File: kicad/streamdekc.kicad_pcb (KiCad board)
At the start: 2 copper layers, 26 parts, among them IC1 74HC4051P, IC2 74HC4051P, SW1 SW_DIP_x01, SW2 SW_DIP_x01, SW3 SW_DIP_x01, SW4 SW_DIP_x01, SW5 SW_DIP_x01, SW6 SW_DIP_x01, SW7 SW_DIP_x01, SW8 SW_DIP_x01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

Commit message: whee
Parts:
- IC1, IC2, U1_1, U1_2, U2_1, U2_2: moved to B.Cu
- moved U1_2 124.5 mm to (82.3, 131.2), turned to -90 degrees
- moved U1_1 116.6 mm to (82.3, 116.0), turned to -90 degrees
- moved U2_2 88.2 mm to (85.0, 106.5), turned to -90 degrees
- moved IC2 87.3 mm to (151.6, 92.7), turned to -90 degrees
- moved IC1 86.3 mm to (116.5, 92.5), turned to -90 degrees
- moved U2_1 72.1 mm to (85.0, 96.2), turned to -90 degrees
- moved SW8 9.50 mm to (207.5, 138.0)

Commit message: Initial pcb design
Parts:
- added REF**: MountingHole_4.3mm_M4_DIN965_Pad, MountingHole:MountingHole_4.3mm_M4_DIN965_Pad, F.Cu at (67.0, 123.5)
- added REF**: MountingHole_4.3mm_M4_DIN965_Pad, MountingHole:MountingHole_4.3mm_M4_DIN965_Pad, F.Cu at (239.0, 68.0)
- added REF**: MountingHole_4.3mm_M4_DIN965_Pad, MountingHole:MountingHole_4.3mm_M4_DIN965_Pad, F.Cu at (67.0, 68.0)
- added REF**: MountingHole_4.3mm_M4_DIN965_Pad, MountingHole:MountingHole_4.3mm_M4_DIN965_Pad, F.Cu at (239.0, 123.5)
- moved IC2 61.7 mm to (91.6, 106.9)
- moved DISP7 33.0 mm to (144.4, 99.7)
- moved U2_2 32.5 mm to (79.5, 74.5), turned to 90 degrees
- moved DISP6 32.1 mm to (112.4, 99.7)
- moved SW3 31.9 mm to (148.2, 92.2)
- moved SW8 31.5 mm to (180.2, 122.2)
- moved DISP5 30.9 mm to (80.4, 99.7)
- moved DISP8 30.8 mm to (176.4, 99.7)
- moved DISP3 30.8 mm to (144.4, 69.7)
- moved SW2 29.9 mm to (116.2, 92.2)
- moved SW4 29.7 mm to (180.2, 92.2)
- moved DISP2 29.5 mm to (112.4, 69.7)
- moved IC1 29.4 mm to (91.1, 77.7)
- moved SW7 29.2 mm to (148.2, 122.2)
- moved DISP4 29.1 mm to (176.4, 69.7)
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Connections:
- SW1 pad 1: unconnected-(SW1-Pad1) -> /SW1
- SW2 pad 1: unconnected-(SW2-Pad1) -> /SW2
- SW3 pad 1: unconnected-(SW3-Pad1) -> /SW3
- SW4 pad 1: unconnected-(SW4-Pad1) -> /SW4
- SW5 pad 1: unconnected-(SW5-Pad1) -> /SW5
- SW6 pad 1: unconnected-(SW6-Pad1) -> /SW6
- SW7 pad 1: unconnected-(SW7-Pad1) -> /SW7
- SW8 pad 1: unconnected-(SW8-Pad1) -> /SW8
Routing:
- net /3V3: track 0.00 -> 292.3 mm, vias 0 -> 1
- net /SCL_5V: track 0.00 -> 257.9 mm, vias 0 -> 1
- net /A3: track 0.00 -> 227.1 mm, vias 0 -> 1
- net /A2: track 0.00 -> 221.4 mm, vias 0 -> 3
- net /A1: track 0.00 -> 212.3 mm, vias 0 -> 3
- net /A0: track 0.00 -> 203.2 mm, vias 0 -> 3
- net /DISP_8_SDA: track 0.00 -> 109.4 mm, vias 0 -> 1
- net /DISP_4_SDA: track 0.00 -> 103.6 mm, vias 0 -> 1
- net /SW4: track 0.00 -> 91.1 mm, vias 0 -> 2
- net /D10: track 0.00 -> 90.8 mm, vias 0 -> 2
- net /D8: track 0.00 -> 90.7 mm, vias 0 -> 2
- net /D9: track 0.00 -> 90.6 mm, vias 0 -> 2
- net /SW3: track 0.00 -> 88.6 mm, vias 0 -> 1
- net /SW8: track 0.00 -> 84.2 mm
- net /DISP_7_SDA: track 0.00 -> 79.5 mm, vias 0 -> 2
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- added copper zone on F.Cu, net /5V
- added copper zone on B.Cu, net /GND
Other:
- board outline added: 184 x 67.5 mm
- board text added: "Order of Assembly: 1. Switches 2. ICs 3. Power Converter 4. Slide Potentiometers 5. Qt Py 6. Displays (Good luck)"
- board text added: "Streamdekc Designed by Mark Hutcheson April 2022"

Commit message: Move QtPy for easier (aka physically possible) assembly
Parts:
- moved U1_1 5.27 mm to (64.5, 102.2)
- moved U1_2 5.27 mm to (64.5, 117.5)
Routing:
- net /D6: track 28.2 -> 35.3 mm, vias 2 -> 3
- net /A3: track 227.1 -> 221.8 mm, vias 1 -> 3
- net /SDA: track 13.2 -> 18.5 mm, vias 0 -> 1
- net /SCL: track 13.4 -> 18.7 mm, vias 0 -> 1
- net /A2: track 221.4 -> 216.1 mm
- net /A1: track 212.3 -> 207.0 mm
- net /A0: track 203.2 -> 198.0 mm
- net /D10: track 90.8 -> 94.7 mm
- net /3V3: track 292.3 -> 295.9 mm, vias 1 -> 2
- net /SCL_5V: track 257.9 -> 261.4 mm
- net /D9: track 90.6 -> 93.2 mm
- net /SW1: track 44.4 -> 46.5 mm
- net /D8: track 90.7 -> 92.3 mm
- net /DISP_5_SDA: track 23.3 -> 24.5 mm
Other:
- board text added: "Order of Assembly: 1. Switches 2. ICs 3. Power Converter 4. Slide Potentiometers 5. Qt Py 6. Displays"
- board text removed: "Order of Assembly: 1. Switches 2. ICs 3. Power Converter 4. Slide Potentiometers 5. Qt Py 6. Displays (Good luck)"

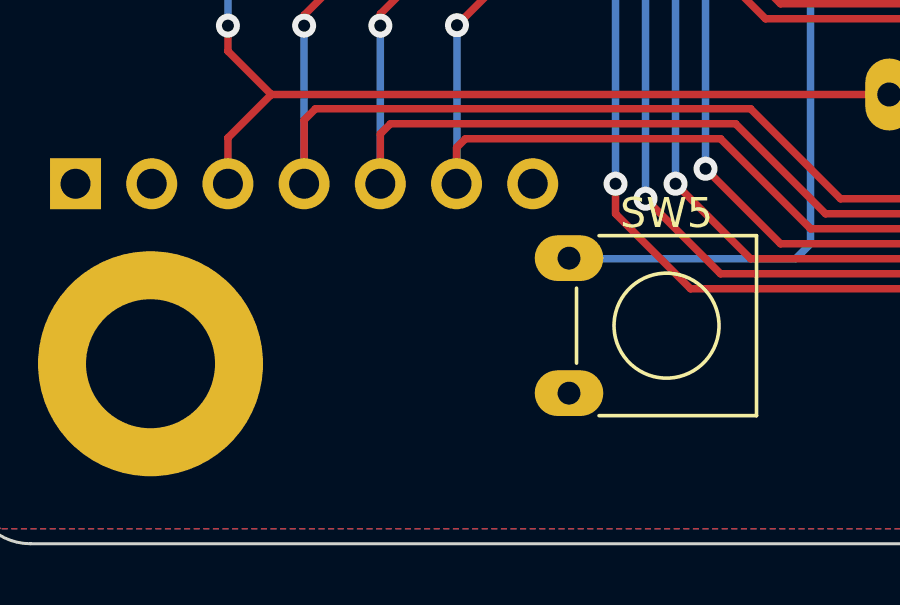
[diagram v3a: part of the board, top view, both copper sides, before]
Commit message: Update assembly instructions on B.Silkscreen
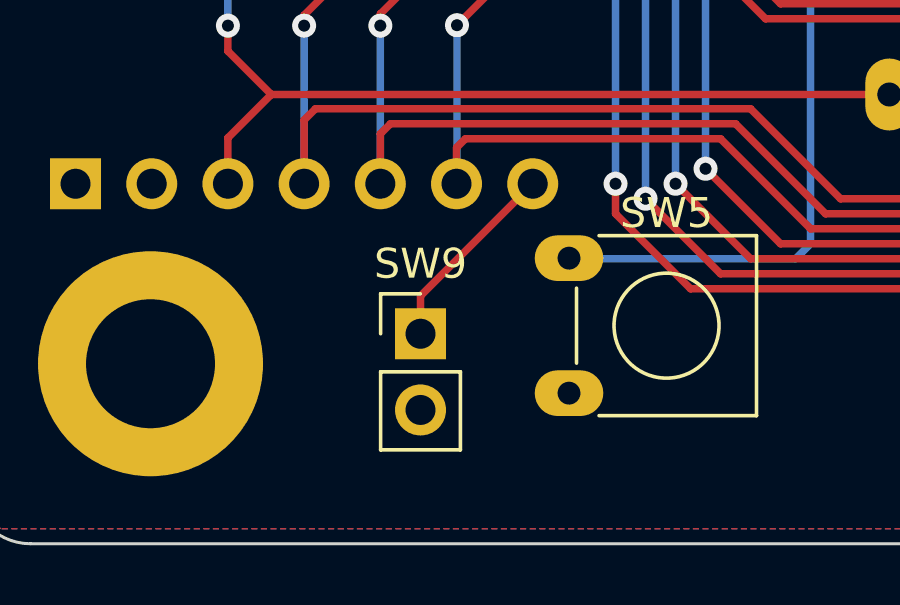
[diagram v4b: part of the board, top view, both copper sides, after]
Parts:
- added SW9: SW_DIP_x01, Connector_PinHeader_2.54mm:PinHeader_1x02_P2.54mm_Vertical, F.Cu at (76.0, 122.5)
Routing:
- net /D7: track 0.00 -> 6.55 mm
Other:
- board text added: "Order of Assembly: 1. Switches 2. ICs 3. Power Converter 4. Slide Potentiometers 5. Qt Py 6. Extra Pin Header 7. Displays"
- board text removed: "Order of Assembly: 1. Switches 2. ICs 3. Power Converter 4. Slide Potentiometers 5. Qt Py 6. Displays"
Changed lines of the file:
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@@
   (net 39 "unconnected-(U2_2-Pad4)")
   (net 40 "unconnected-(U2_2-Pad5)")
+  (footprint "Connector_PinHeader_2.54mm:PinHeader_1x02_P2.54mm_Vertical" (layer "F.Cu")
+    (at 76 122.5)
+    (descr "Through hole straight pin header, 1x02, 2.54mm pitch, single row")
+    (tags "Through hole pin header THT 1x02 2.54mm single row")
+    (property "Sheetfile" "streamdekc.kicad_sch")
+    (property "Sheetname" "")
+    (attr through_hole)
+    (fp_text reference "SW9" (at 0 -2.33) (layer "F.SilkS")
+      (effects (font (size 1 1) (thickness 0.15)))
+    )
+    (fp_text value "SW_DIP_x01" (at 0 4.87) (layer "F.Fab")
+      (effects (font (size 1 1) (thickness 0.15)))
+    )
+    (fp_text user "${REFERENCE}" (at 0 1.27 90) (layer "F.Fab")
+      (effects (font (size 1 1) (thickness 0.15)))
+    )
+    (fp_line (start -1.33 1.27) (end 1.33 1.27) (layer "F.SilkS") (width 0.12))
+    (fp_line (start -1.33 1.27) (end -1.33 3.87) (layer "F.SilkS") (width 0.12))
+    (fp_line (start -1.33 -1.33) (end 0 -1.33) (layer "F.SilkS") (width 0.12))
+    (fp_line (start 1.33 1.27) (end 1.33 3.87) (layer "F.SilkS") (width 0.12))
+    (fp_line (start -1.33 3.87) (end 1.33 3.87) (layer "F.SilkS") (width 0.12))
+    (fp_line (start -1.33 0) (end -1.33 -1.33) (layer "F.SilkS") (width 0.12))
+    (fp_line (start 1.8 4.35) (end 1.8 -1.8) (layer "F.CrtYd") (width 0.05))
+    (fp_line (start -1.8 -1.8) (end -1.8 4.35) (layer "F.CrtYd") (width 0.05))
+    (fp_line (start -1.8 4.35) (end 1.8 4.35) (layer "F.CrtYd") (width 0.05))
+    (fp_line (start 1.8 -1.8) (end -1.8 -1.8) (layer "F.CrtYd") (width 0.05))
+    (fp_line (start -0.635 -1.27) (end 1.27 -1.27) (layer "F.Fab") (width 0.1))
+    (fp_line (start -1.27 -0.635) (end -0.635 -1.27) (layer "F.Fab") (width 0.1))
+    (fp_line (start -1.27 3.81) (end -1.27 -0.635) (layer "F.Fab") (width 0.1))
+    (fp_line (start 1.27 -1.27) (end 1.27 3.81) (layer "F.Fab") (width 0.1))
+    (fp_line (start 1.27 3.81) (end -1.27 3.81) (layer "F.Fab") (width 0.1))
+    (pad "1" thru_hole rect locked (at 0 0) (size 1.7 1.7) (drill 1) (layers *.Cu *.Mask)
+      (net 14 "/D7") (pintype "passive"))
+    (pad "2" thru_hole oval locked (at 0 2.54) (size 1.7 1.7) (drill 1) (layers *.Cu *.Mask)
+      (net 3 "/GND") (pintype "passive"))
+    (model "${KICAD6_3DMODEL_DIR}/Connector_PinHeader_2.54mm.3dshapes/PinHeader_1x02_P2.54mm_Vertical.wrl"
+      (offset (xyz 0 0 0))
+      (scale (xyz 1 1 1))
+      (rotate (xyz 0 0 0))
+    )
+  )
   (footprint "MountingHole:MountingHole_4.3mm_M4_DIN965_Pad" (layer "F.Cu")
     (at 67 123.5)
@@
   (gr_arc (start 63 129.5) (mid 61.585786 128.914214) (end 61 127.5) (layer "Edge.Cuts") (width 0.1))
   (gr_arc (start 243 62) (mid 244.414214 62.585786) (end 245 64) (layer "Edge.Cuts") (width 0.1))
-  (gr_text "Order of Assembly:\n1. Switches\n2. ICs\n3. Power Converter\n4. Slide Potentiometers\n5. Qt Py\n6. Displays" (at 142 82) (layer "B.SilkS")
+  (gr_text "Order of Assembly:\n1. Switches\n2. ICs\n3. Power Converter\n4. Slide Potentiometers\n5. Qt Py\n6. Extra Pin Header\n7. Displays" (at 141 81) (layer "B.SilkS")
     (effects (font (size 1 1) (thickness 0.15)) (justify left mirror))
   )
@@
   (segment (start 109 85.445) (end 108.905 85.35) (width 0.25) (layer "B.Cu") (net 13))
   (segment (start 77.2 117.5) (end 77.215 117.485) (width 0.25) (layer "B.Cu") (net 13))
+  (segment (start 76 121.24) (end 76 122.5) (width 0.25) (layer "F.Cu") (net 14))
+  (segment (start 79.74 117.5) (end 76 121.24) (width 0.25) (layer "F.Cu") (net 14))
   (segment (start 85.48 97.52) (end 115.27 97.52) (width 0.25) (layer "F.Cu") (net 15))
   (segment (start 146.75 67) (end 178.75 67) (width 0.25) (layer "F.Cu") (net 15))
